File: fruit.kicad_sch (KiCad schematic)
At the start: 7 parts, among them J1 ERM8-030-01-L-D-RA-TR

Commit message: respin
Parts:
- removed J1: ERM8-030-01-L-D-RA-TR, Connector_Header_Samtec:SAMTEC_ERM8-030-01-L-D-RA-TR, symbol Connector_Header_Samtec:ERM8-030-01-L-D-RA-TR
- added J1: PCB_Edge_PCI_Express_x4_Salmonberry, Connector_PCIe_MyOwn:BUS_PCIexpress_x4_Salmonberry_reduced_shoulders, symbol Connector_PCIe_MyOwn:PCB_Edge_PCI_Express_x4_Salmonberry
- H1, H2: footprint MountingHole:MountingHole_2.5mm_Pad_TopBottom -> MountingHole:MountingHole_2.7mm_M2.5; symbol Mechanical:MountingHole_Pad -> Mechanical:MountingHole
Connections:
- net GND: now also J1.A1 (~{PRSNT#1}), J1.A10 (GND), J1.A12 (GND), J1.A14 (GND), J1.A15 (GND), J1.A18 (GND), J1.A19 (GND), J1.A20 (GND), J1.A23 (GND), J1.A24 (GND), J1.A27 (GND), J1.A28 (GND), J1.A29 (GND), J1.A30 (GND), J1.A31 (GND), J1.A32 (GND), J1.A4 (GND), J1.A7 (GND), J1.A8 (GND), J1.B11 (GND), J1.B12 (GND), J1.B13 (GND), J1.B16 (GND), J1.B17 (~{PRSNT#2}), J1.B18 (GND), J1.B21 (GND), J1.B22 (GND), J1.B25 (GND), J1.B26 (GND), J1.B29 (GND), J1.B30 (GND), J1.B31 (~{PRSNT#3}), J1.B32 (GND), J1.B4 (GND), J1.B7 (GND), J1.B9 (GND); no longer H1.1, H2.1
- net ~{I2C_RESET}: now also J1.A13 (~{I2C_RST1})
- new net +12V: J1.A2 (+12V), J1.A3 (+12V), J1.B1 (+12V), J1.B2 (+12V), J1.B3 (+12V)
- new net +3.3V: J1.A5 (+3.3V), J1.A6 (+3.3V), J1.B5 (+3.3V), J1.B6 (+3.3V)
- new net EthA+: J1.B19 (EthA1+)
- new net EthA-: J1.B20 (EthA1-)
- new net EthB+: J1.A21 (EthB1+)
- new net EthB-: J1.A22 (EthB1-)
- new net EthC+: J1.B23 (EthC1+)
- new net EthC-: J1.B24 (EthC1-)
- new net EthD+: J1.A25 (EthD1+)
- new net EthD-: J1.A26 (EthD1-)
- new net I2C_SCL: J1.B8 (SCL)
- new net I2C_SDA: J1.B10 (SDA)
- new net UART_CTS1: J1.A17 (UART_CTS1)
- new net UART_RTS1: J1.A16 (UART_RTS1)
- new net UART_RXD1: J1.B15 (UART_RX1)
- new net UART_TXD1: J1.B14 (UART_TX1)
- new net USB1+: J1.B27 (USB1+)
- new net USB1-: J1.B28 (USB1-)
- no-connect marks 8 -> 5
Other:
- sheet Fruit ports: added +12V_IN, +3.3V_CONTROL, I2C_SCL, I2C_SDA, UART_CTS1, UART_RTS1, UART_RXD1, UART_TXD1, ~{PRSNT_BOARD_X1_1}, ~{PRSNT_BOARD_X4_1}, ~{PRSNT_BOARD_X8_1}; removed +12V_A_IN, +12V_B_IN, CONTROL_+3.3V, FRUIT_PANIC, HB_LED, I2C_CM4_SCL, I2C_CM4_SDA, UART_CTS0, UART_RTS0, UART_RXD0, UART_TXD0
- note removed: "+3.3V"
- note removed: "+5V"
- note removed: "Plug"
- note removed: "Reserved"
- note removed: "USB+"
- note removed: "USB-"

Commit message: respin
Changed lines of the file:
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@@
     (stroke (width 0) (type solid) (color 0 0 0 0))
   )
-  (wire (pts (xy 16.51 138.43) (xy 36.83 138.43))
+  (wire (pts (xy 125.73 157.48) (xy 146.05 157.48))
     (stroke (width 0) (type default) (color 0 0 0 0))
   )
@@
     (stroke (width 0) (type default) (color 0 0 0 0))
   )
-  (wire (pts (xy 16.51 146.05) (xy 36.83 146.05))
+  (wire (pts (xy 125.73 165.1) (xy 146.05 165.1))
     (stroke (width 0) (type default) (color 0 0 0 0))
   )
@@
     (effects (font (size 1.27 1.27)) (justify right bottom))
   )
-  (label "+3.3V_CONTROL" (at 16.51 146.05 0)
+  (label "+3.3V_CONTROL" (at 125.73 165.1 0)
     (effects (font (size 1.27 1.27)) (justify left bottom))
   )
@@
     (effects (font (size 1.27 1.27)) (justify right bottom))
   )
-  (label "+12V_IN" (at 16.51 138.43 0)
+  (label "+12V_IN" (at 125.73 157.48 0)
     (effects (font (size 1.27 1.27)) (justify left bottom))
   )
@@
     (pin "1")
   )
-  (symbol (lib_id "power:PWR_FLAG") (at 36.83 146.05 0) (unit 1)
+  (symbol (lib_id "power:PWR_FLAG") (at 146.05 165.1 0) (unit 1)
     (in_bom yes) (on_board yes)
-    (property "Reference" "#FLG02" (id 0) (at 36.83 144.145 0)
-      (effects (font (size 1.27 1.27)) hide)
-    )
-    (property "Value" "PWR_FLAG" (id 1) (at 36.83 142.24 0))
-    (property "Footprint" "" (id 2) (at 36.83 146.05 0)
-      (effects (font (size 1.27 1.27)) hide)
-    )
-    (property "Datasheet" "~" (id 3) (at 36.83 146.05 0)
+    (property "Reference" "#FLG02" (id 0) (at 146.05 163.195 0)
+      (effects (font (size 1.27 1.27)) hide)
+    )
+    (property "Value" "PWR_FLAG" (id 1) (at 146.05 161.29 0))
+    (property "Footprint" "" (id 2) (at 146.05 165.1 0)
+      (effects (font (size 1.27 1.27)) hide)
+    )
+    (property "Datasheet" "~" (id 3) (at 146.05 165.1 0)
       (effects (font (size 1.27 1.27)) hide)
     )
     (pin "1")
   )
-  (symbol (lib_id "power:PWR_FLAG") (at 36.83 138.43 0) (unit 1)
+  (symbol (lib_id "power:PWR_FLAG") (at 146.05 157.48 0) (unit 1)
     (in_bom yes) (on_board yes)
-    (property "Reference" "#FLG01" (id 0) (at 36.83 136.525 0)
-      (effects (font (size 1.27 1.27)) hide)
-    )
-    (property "Value" "PWR_FLAG" (id 1) (at 36.83 134.62 0))
-    (property "Footprint" "" (id 2) (at 36.83 138.43 0)
-      (effects (font (size 1.27 1.27)) hide)
-    )
-    (property "Datasheet" "~" (id 3) (at 36.83 138.43 0)
-      (effects (font (size 1.27 1.27)) hide)
-    )
+    (property "Reference" "#FLG01" (id 0) (at 146.05 155.575 0)
+      (effects (font (size 1.27 1.27)) hide)
+    )
+    (property "Value" "PWR_FLAG" (id 1) (at 146.05 153.67 0))
+    (property "Footprint" "" (id 2) (at 146.05 157.48 0)
+      (effects (font (size 1.27 1.27)) hide)
+    )
+    (property "Datasheet" "~" (id 3) (at 146.05 157.48 0)
+      (effects (font (size 1.27 1.27)) hide)
+    )

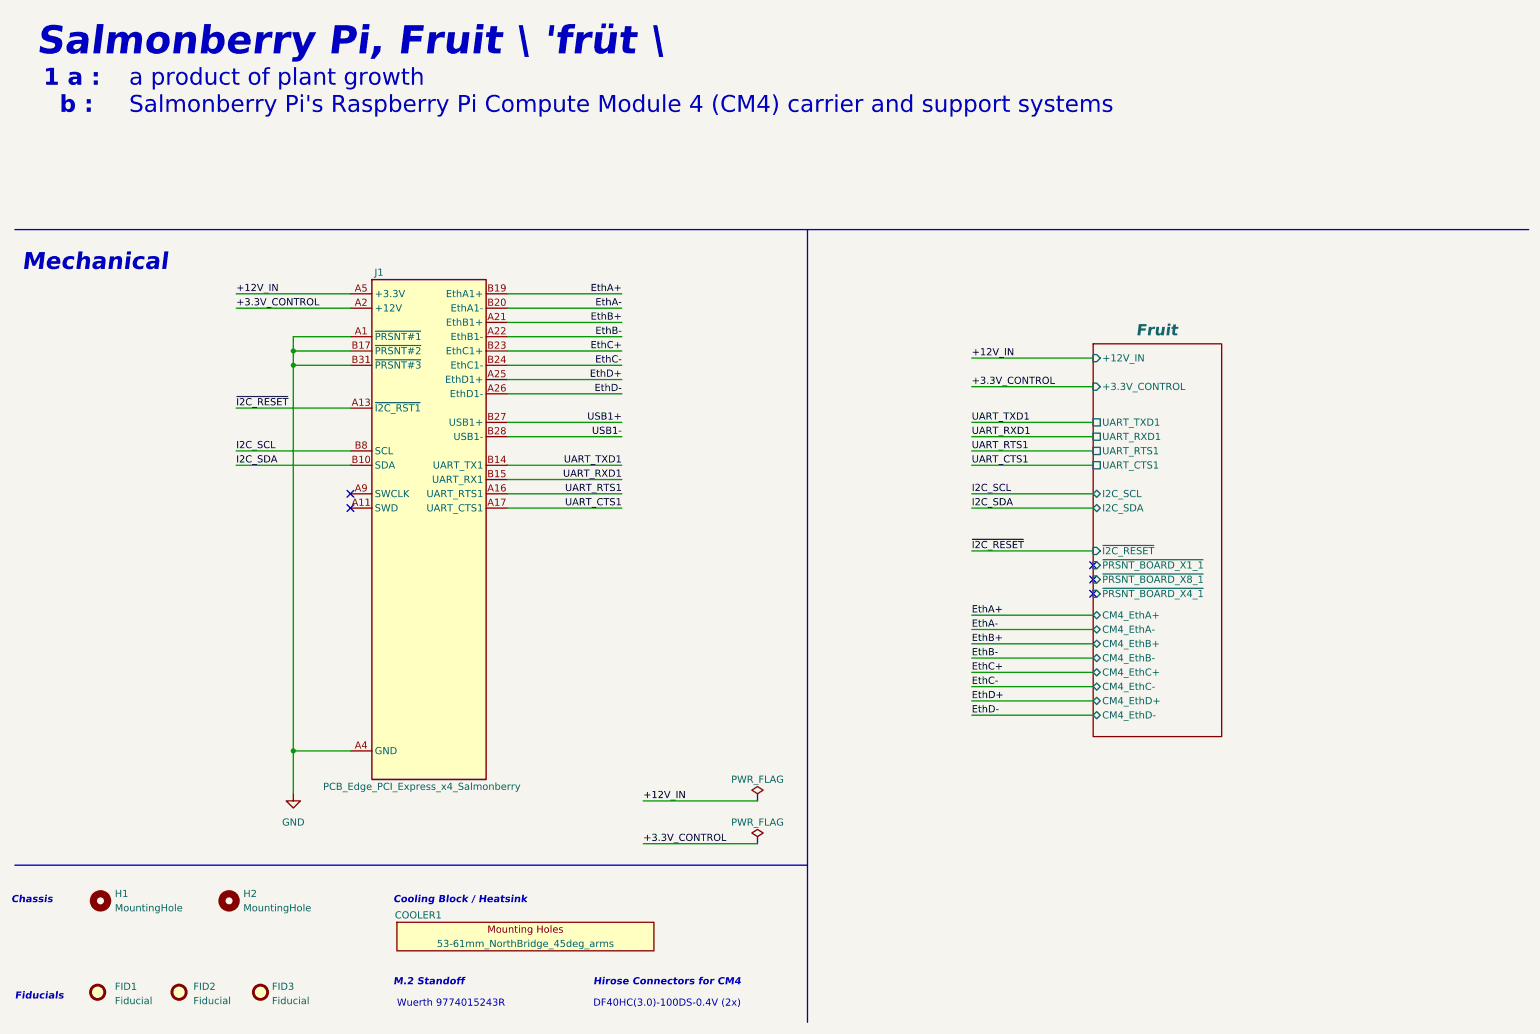
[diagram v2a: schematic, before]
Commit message: fixed I2C ping indicator
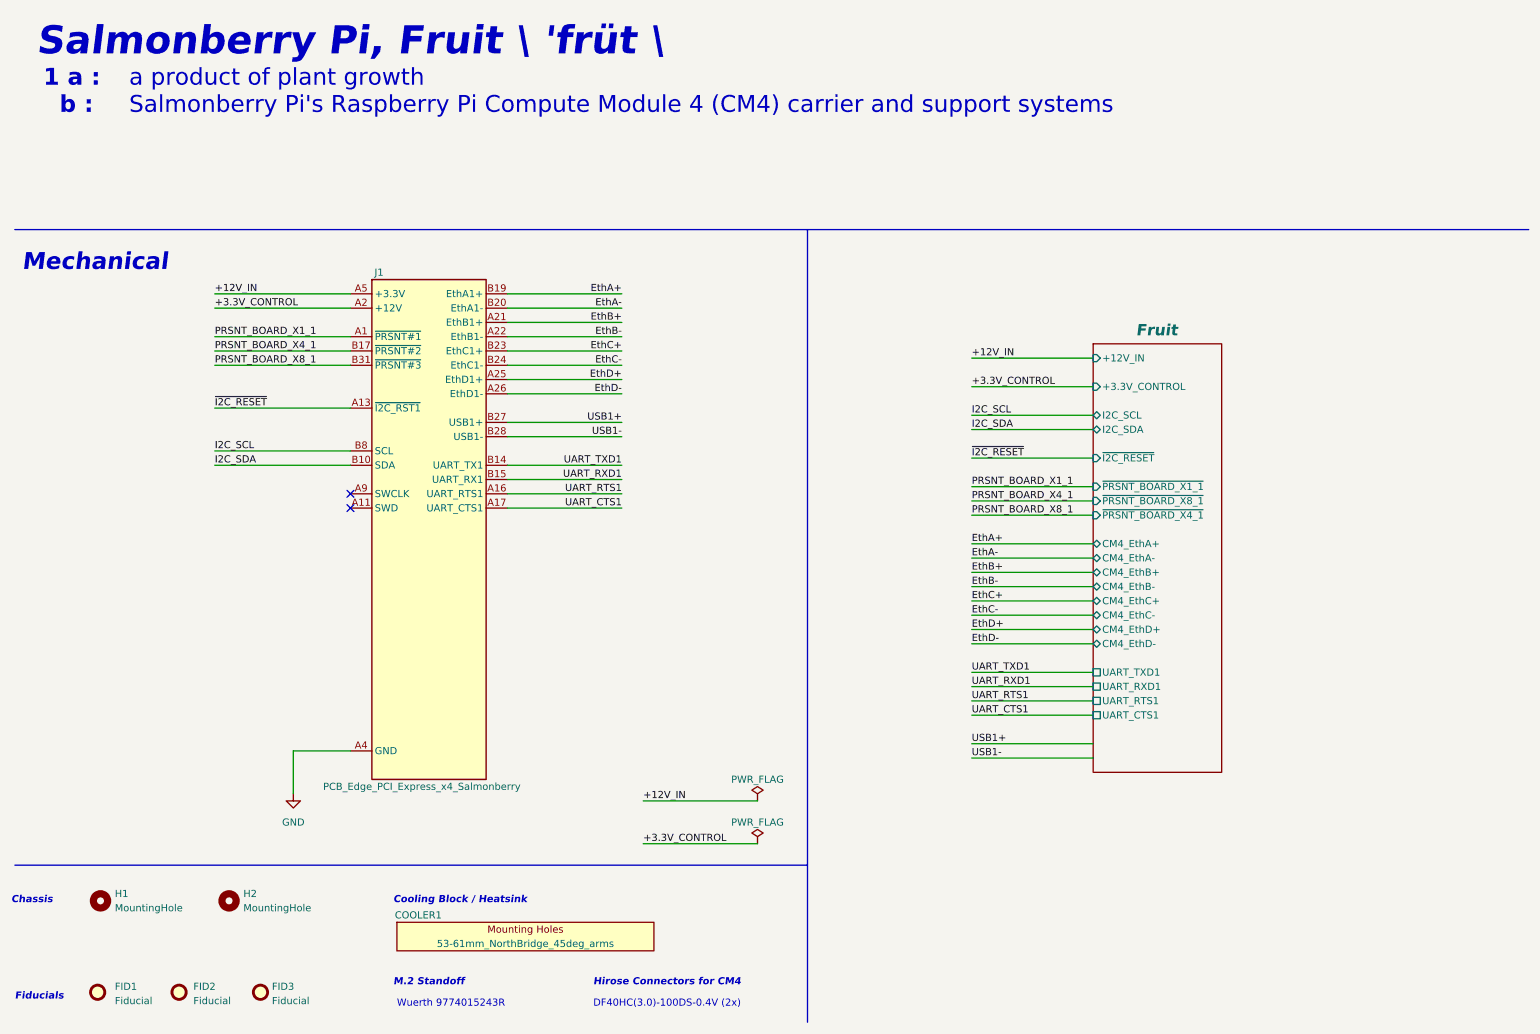
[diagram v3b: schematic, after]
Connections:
- net GND: no longer J1.A1 (~{PRSNT#1}), J1.B17 (~{PRSNT#2}), J1.B31 (~{PRSNT#3})
- new net PRSNT_BOARD_X1_1: J1.A1 (~{PRSNT#1})
- new net PRSNT_BOARD_X4_1: J1.B17 (~{PRSNT#2})
- new net PRSNT_BOARD_X8_1: J1.B31 (~{PRSNT#3})
- no-connect marks 5 -> 2
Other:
- title: Salmonberry Pi, Fruit \ 'früt \ -> Salmonberry Pi, Fruit \ 'früt \ CM4

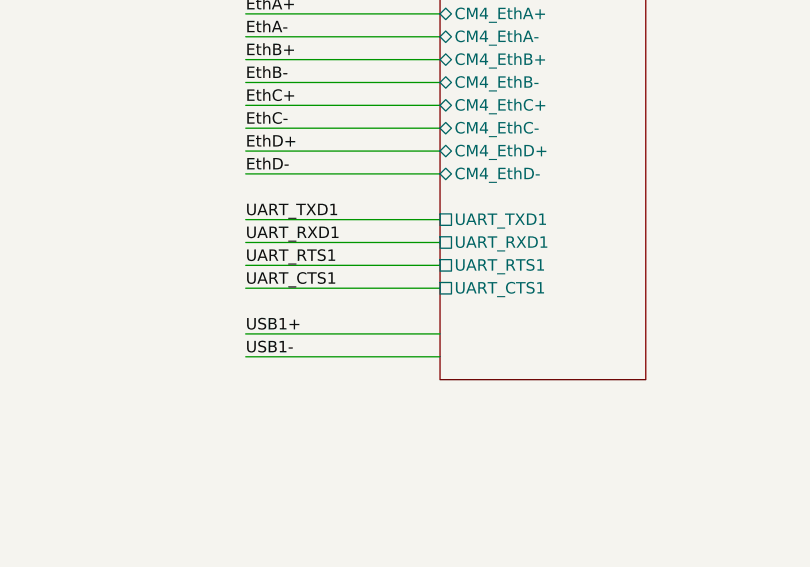
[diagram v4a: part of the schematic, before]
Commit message: added ti buffer lib
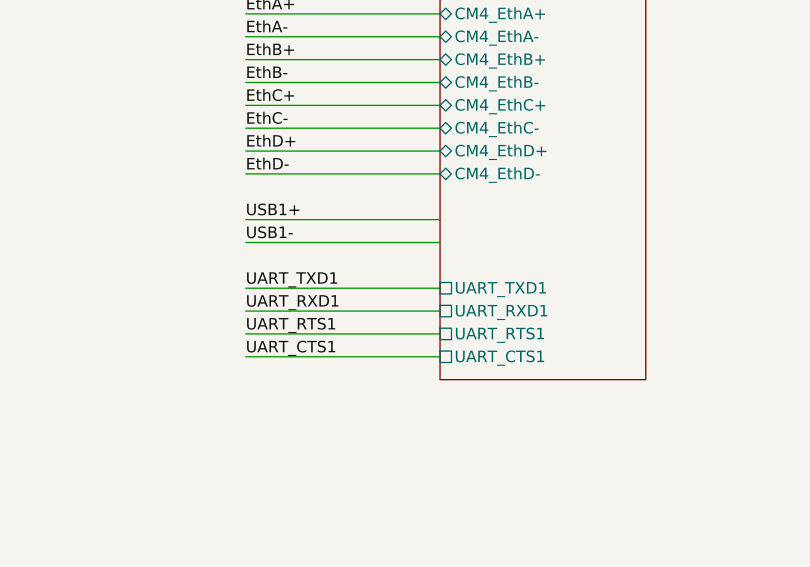
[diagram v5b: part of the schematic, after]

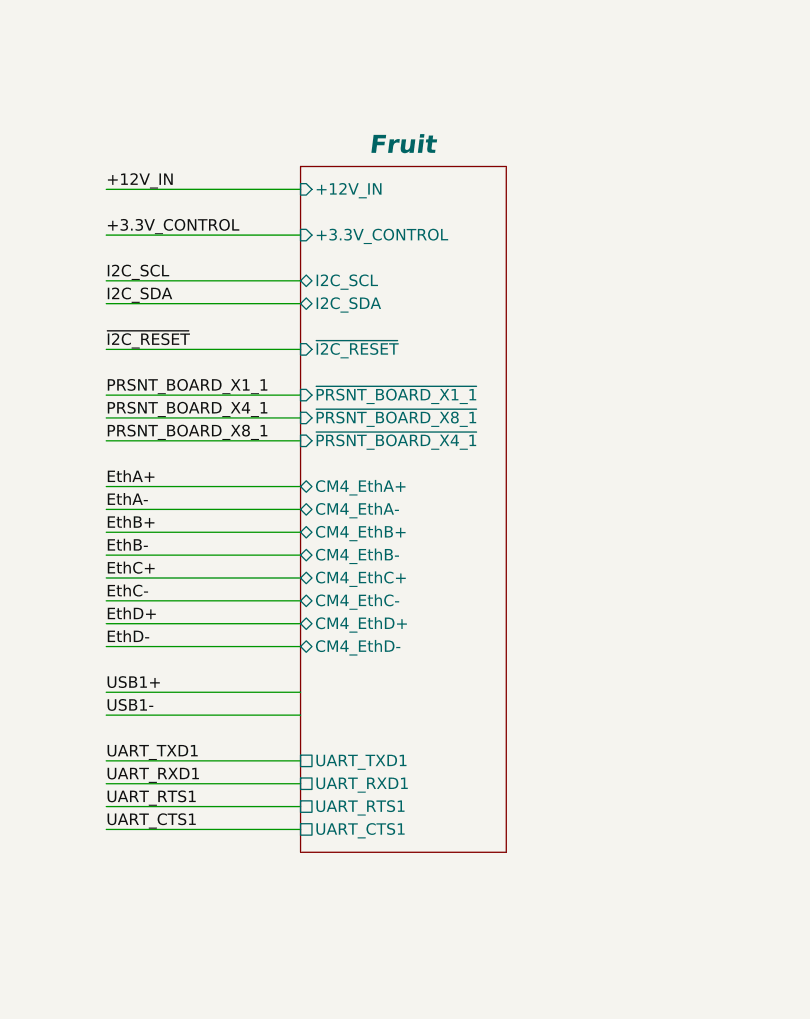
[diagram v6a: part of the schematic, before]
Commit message: initial integration of i2c arbiter
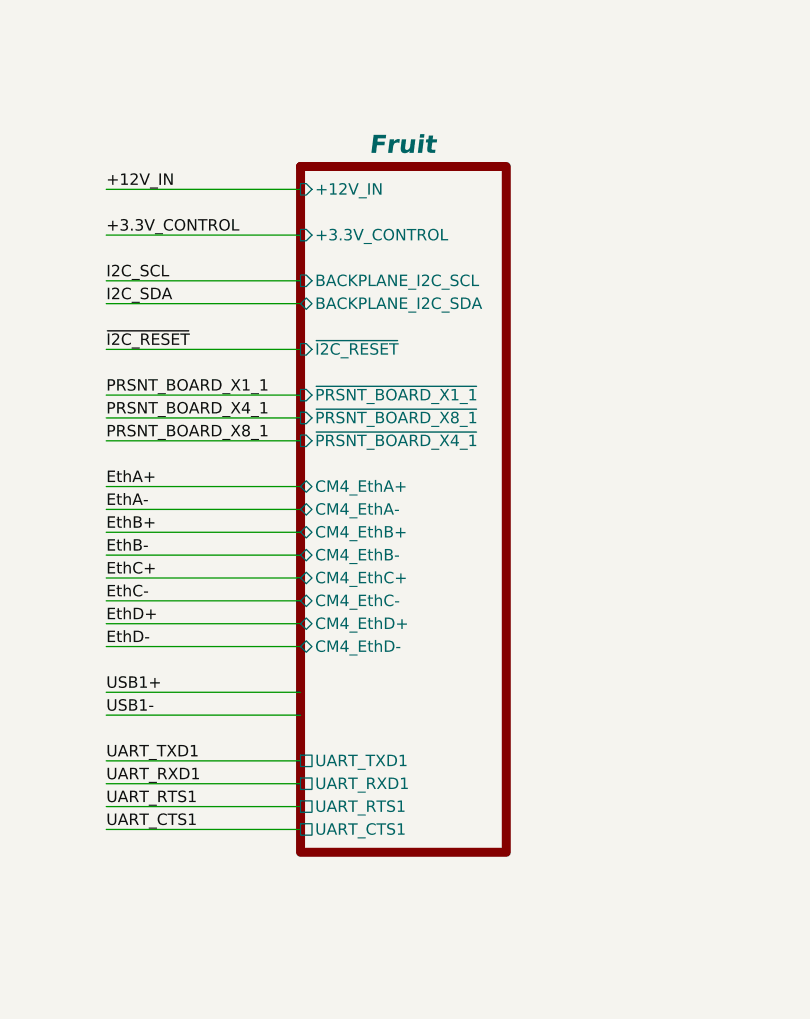
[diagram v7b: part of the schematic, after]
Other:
- sheet Fruit ports: added BACKPLANE_I2C_SCL, BACKPLANE_I2C_SDA; removed I2C_SCL, I2C_SDA
